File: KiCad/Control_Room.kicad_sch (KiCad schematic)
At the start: 14 parts, among them U1 MAX485E, U2 MAX485E

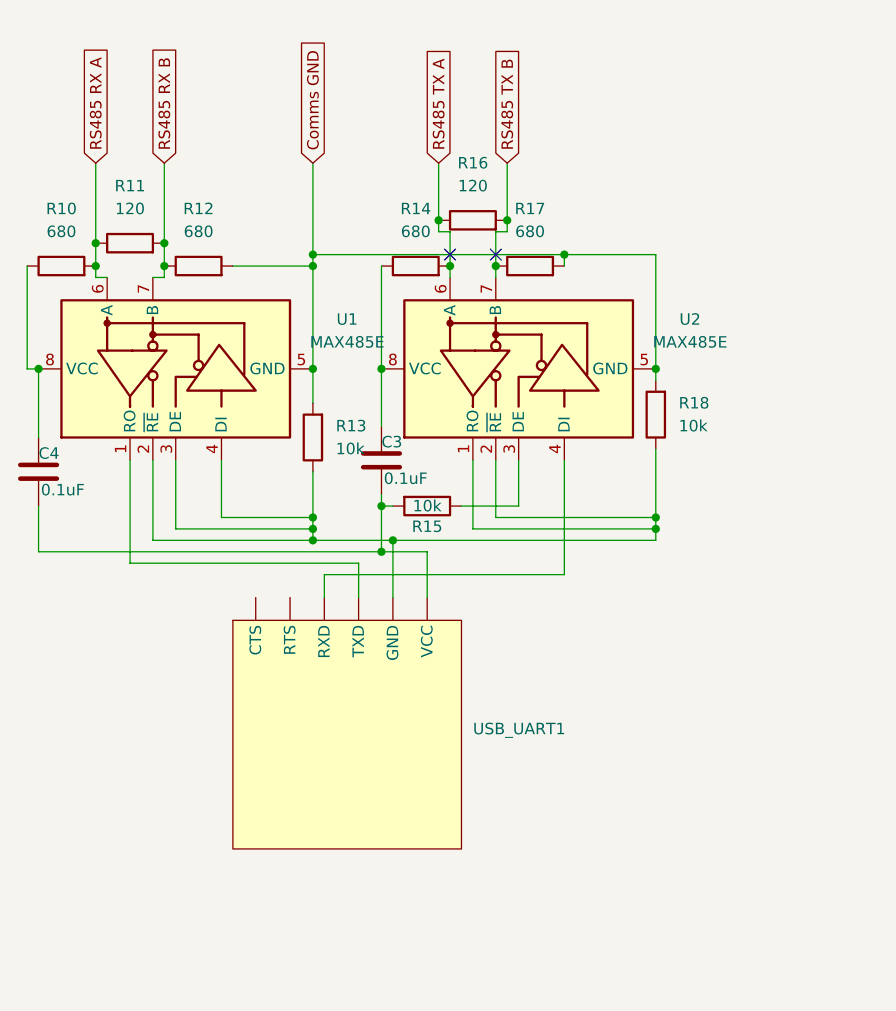
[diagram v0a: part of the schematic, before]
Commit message: Update Schematic to remove unneeded caps and resistors
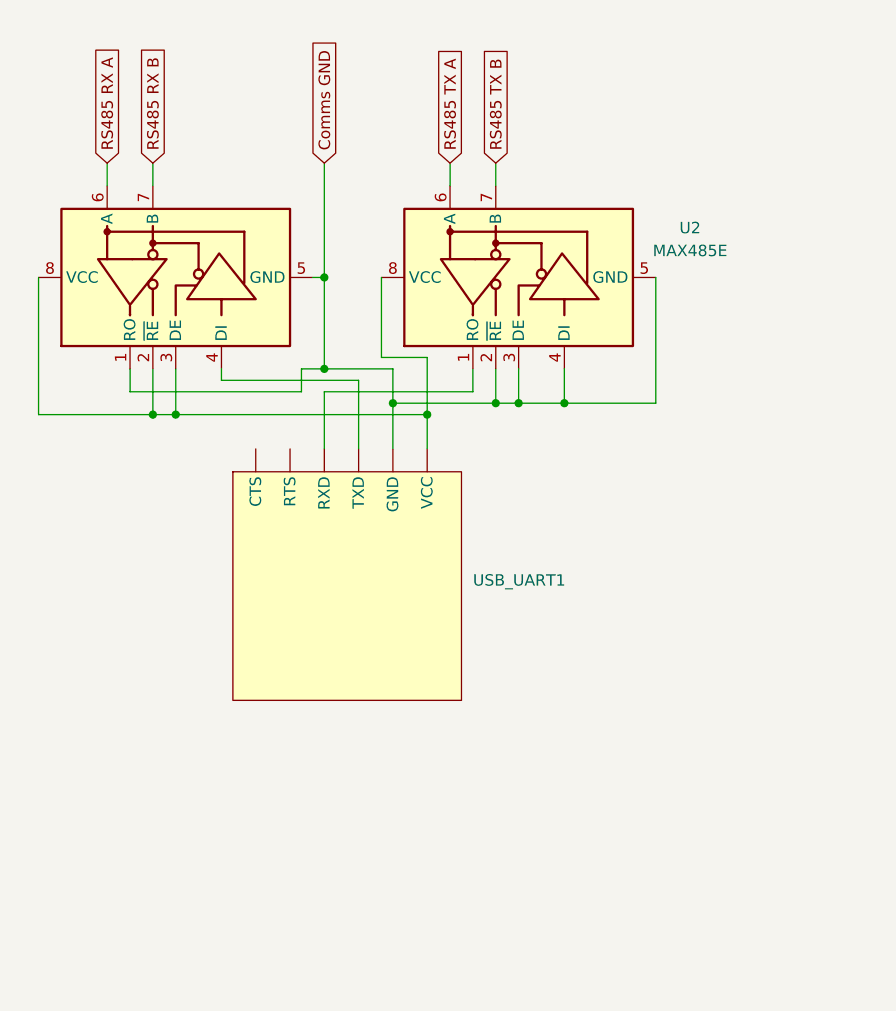
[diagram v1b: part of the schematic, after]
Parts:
- removed C3, C4: 0.1uF, symbol Device:C
- removed R10, R12, R14, R17: 680, symbol Device:R
- removed R11, R16: 120, symbol Device:R
- removed R13, R15, R18: 10k, symbol Device:R
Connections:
- net Comms GND: now also U1.1 (RO), U2.2 (~{RE}), U2.3 (DE), U2.4 (DI), USB_UART1. (VCC)
- net at U2.8 (VCC): now also U1.2 (~{RE}), U1.3 (DE), U1.8 (VCC), USB_UART1. (VCC)
- new net: U1.4 (DI), USB_UART1. (VCC)
- new net: U2.1 (RO), USB_UART1. (VCC)
- no-connect marks 2 -> 0
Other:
- moved on the sheet: U2, USB_UART1

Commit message: PCB Layout V1
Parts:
- removed USB_UART1: ~, symbol USB_UART:USB_UART
- added J_USB_DATA1: TX_RX, symbol Connector:Screw_Terminal_01x02
- added J_USB_POWER1: Power, symbol Connector:Screw_Terminal_01x02
- U1, U2: footprint Package_SO:SOIC-8_3.9x4.9mm_P1.27mm -> (none)
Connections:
- net Comms GND: now also J_USB_POWER1.2 (Pin_2)
- net at U1.2 (~{RE}), U1.3 (DE), U1.8 (VCC)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: now also J_USB_POWER1.1 (Pin_1)
- net at U1.4 (DI): now also J_USB_DATA1.1 (Pin_1)
- net at U2.1 (RO): now also J_USB_DATA1.2 (Pin_2)
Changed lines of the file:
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@@
 	(paper "A4")
 	(junction
-		(at 133.35 41.91)
-		(diameter 0)
-		(color 0 0 0 0)
-	)
-	(junction
 		(at 116.84 57.15)
 		(diameter 0)
@@
 	)
 	(junction
+		(at 133.35 41.91)
+		(diameter 0)
+		(color 0 0 0 0)
+	)
+	(junction
 		(at 114.3 57.15)
 		(diameter 0)
@@
 	(wire
 		(pts
-			(xy 101.6 57.15) (xy 114.3 57.15)
-		)
-		(stroke
-			(width 0)
-			(type default)
-		)
-	)
-	(wire
-		(pts
-			(xy 140.97 55.88) (xy 140.97 60.96)
+			(xy 142.24 60.96) (xy 142.24 63.5)
 		)
 		(stroke
@@
 	(wire
 		(pts
-			(xy 111.76 52.07) (xy 111.76 54.61)
+			(xy 101.6 57.15) (xy 114.3 57.15)
 		)
 		(stroke
@@
 	(wire
 		(pts
-			(xy 132.08 41.91) (xy 133.35 41.91)
+			(xy 140.97 55.88) (xy 140.97 60.96)
 		)
 		(stroke
@@
 	(wire
 		(pts
-			(xy 137.16 53.34) (xy 137.16 60.96)
+			(xy 137.16 53.34) (xy 137.16 63.5)
 		)
 		(stroke
@@
 	(wire
 		(pts
+			(xy 132.08 41.91) (xy 133.35 41.91)
+		)
+		(stroke
+			(width 0)
+			(type default)
+		)
+	)
+	(wire
+		(pts
 			(xy 133.35 41.91) (xy 133.35 52.07)
 		)
@@
 	(wire
 		(pts
-			(xy 144.78 60.96) (xy 144.78 57.15)
+			(xy 101.6 41.91) (xy 101.6 57.15)
 		)
 		(stroke
@@
 	(wire
 		(pts
+			(xy 111.76 52.07) (xy 111.76 54.61)
+		)
+		(stroke
+			(width 0)
+			(type default)
+		)
+	)
+	(wire
+		(pts
+			(xy 144.78 57.15) (xy 144.78 63.5)
+		)
+		(stroke
+			(width 0)
+			(type default)
+		)
+	)
+	(wire
+		(pts
+			(xy 133.35 60.96) (xy 134.62 60.96)
+		)
+		(stroke
+			(width 0)
+			(type default)
+		)
+	)
+	(wire
+		(pts
 			(xy 149.86 54.61) (xy 133.35 54.61)
 		)
@@
 	(wire
 		(pts
-			(xy 114.3 29.21) (xy 114.3 31.75)
+			(xy 140.97 60.96) (xy 142.24 60.96)
 		)
 		(stroke
@@
 	(wire
 		(pts
-			(xy 101.6 57.15) (xy 101.6 41.91)
+			(xy 134.62 60.96) (xy 134.62 63.5)
+		)
+		(stroke
+			(width 0)
+			(type default)
+		)
+	)
+	(wire
+		(pts
+			(xy 114.3 29.21) (xy 114.3 31.75)
 		)
 		(stroke
@@
 			)
 		)
-		(property "Footprint" "Package_SO:SOIC-8_3.9x4.9mm_P1.27mm"
+		(property "Footprint" ""
 			(at 139.7 41.91 0)
 			(effects
@@
 	)
 	(symbol
+		(lib_id "Connector:Screw_Terminal_01x02")
+		(at 144.78 68.58 270)
+		(unit 1)
+		(exclude_from_sim no)
+		(in_bom yes)
+		(on_board yes)
+		(dnp no)
+		(property "Reference" "J_USB_POWER1"
+			(at 142.748 72.136 90)
+			(effects
+				(font
+					(size 1.27 1.27)
+				)
+				(justify left)
+			)
+		)
+		(property "Value" "Power"
+			(at 147.066 68.072 90)
+			(effects
+				(font
+					(size 1.27 1.27)
+				)
+				(justify left)
+			)
+		)
+		(property "Footprint" ""
+			(at 144.78 68.58 0)
+			(effects
+				(font
+					(size 1.27 1.27)
+				)
+				(hide yes)
+			)
+		)
+		(property "Datasheet" "~"
+			(at 144.78 68.58 0)
+			(effects
+				(font
+					(size 1.27 1.27)
+				)
+				(hide yes)
+			)
+		)
+		(property "Description" "Generic screw terminal, single row, 01x02, script generated (kicad-library-utils/schlib/autogen/connector/)"
+			(at 144.78 68.58 0)
+			(effects
+				(font
+					(size 1.27 1.27)
+				)
+				(hide yes)
+			)
+		)
+		(pin "2"
+		)
+		(pin "1"
+		)
+		(instances
+			(project ""
+				(path "/4e05caf8-77e4-4a22-9a05-51fcca8e50ff/b15947ff-9075-4e47-b24b-e604669a88aa"
+					(reference "J_USB_POWER1")
+					(unit 1)
+				)
+			)
+		)
+	)
+	(symbol
 		(lib_id "Interface_UART:MAX485E")
 		(at 154.94 41.91 90)
@@
 			)
 		)
-		(property "Footprint" "Package_SO:SOIC-8_3.9x4.9mm_P1.27mm"
+		(property "Footprint" ""
 			(at 177.8 41.91 0)
 			(effects
@@
 	)
 	(symbol
-		(lib_id "USB_UART:USB_UART")
-		(at 135.89 76.2 0)
+		(lib_id "Connector:Screw_Terminal_01x02")
+		(at 137.16 68.58 270)
 		(unit 1)
 		(exclude_from_sim no)
@@
 		(on_board yes)
 		(dnp no)
-		(fields_autoplaced yes)
-		(property "Reference" "USB_UART1"
-			(at 149.86 75.5649 0)
+		(property "Reference" "J_USB_DATA1"
+			(at 121.158 68.58 90)
 			(effects
 				(font
@@
 			)
 		)
-		(property "Value" "~"
-			(at 149.86 77.47 0)
+		(property "Value" "TX_RX"
+			(at 132.842 71.628 90)
 			(effects
 				(font
@@
 		)
 		(property "Footprint" ""
-			(at 135.89 76.2 0)
+			(at 137.16 68.58 0)
 			(effects
 				(font
@@
 			)
 		)
-		(property "Datasheet" ""
-			(at 135.89 76.2 0)
+		(property "Datasheet" "~"
+			(at 137.16 68.58 0)
 			(effects
 				(font
@@
 			)
 		)
-		(property "Description" ""
-			(at 135.89 76.2 0)
+		(property "Description" "Generic screw terminal, single row, 01x02, script generated (kicad-library-utils/schlib/autogen/connector/)"
+			(at 137.16 68.58 0)
 			(effects
 				(font
@@
 			)
 		)
-		(pin ""
-		)
-		(pin ""
-		)
-		(pin ""
-		)
-		(pin ""
-		)
-		(pin ""
+		(pin "2"
 		)
-		(pin ""
+		(pin "1"
 		)
 		(instances
-			(project ""
+			(project "Systems&Electronics"
 				(path "/4e05caf8-77e4-4a22-9a05-51fcca8e50ff/b15947ff-9075-4e47-b24b-e604669a88aa"
-					(reference "USB_UART1")
+					(reference "J_USB_DATA1")
 					(unit 1)
 				)
